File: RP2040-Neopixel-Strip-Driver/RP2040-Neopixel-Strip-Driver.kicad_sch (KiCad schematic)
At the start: 0 parts

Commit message: Added Motor Driver
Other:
- added sheet Motor Driver (DRV8837CDSGR.kicad_sch)
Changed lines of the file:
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@@
+    )
+  )
+  (sheet (at 144.78 130.81) (size 57.15 31.75) (fields_autoplaced)
+    (stroke (width 0.1524) (type solid) (color 0 0 0 0))
+    (fill (color 0 0 0 0.0000))
+    (property "Sheet name" "Motor Driver" (id 0) (at 144.78 130.0984 0)
+      (effects (font (size 1.27 1.27)) (justify left bottom))
+    )
+    (property "Sheet file" "DRV8837CDSGR.kicad_sch" (id 1) (at 144.78 163.1446 0)
+      (effects (font (size 1.27 1.27)) (justify left top))
     )
   )
@@
     (path "/7d3ce60b-0fbc-4d1c-8ad6-57910cd4368e" (page "7"))
     (path "/84db7bec-6432-452c-8477-921546ad9ffb" (page "8"))
+    (path "/855ed567-09e1-4ac3-90b0-f7e25f211a13" (page "9"))
   )
   (symbol_instances
@@
       (reference "U?") (unit 1) (value "S15OT421-005") (footprint "")
     )
+    (path "/855ed567-09e1-4ac3-90b0-f7e25f211a13/a4fd550c-a752-48e0-8fc2-29b1df7424eb"
+      (reference "U?") (unit 1) (value "DRV8837CDSGR") (footprint "SON50P200X200X80-9N")
+    )
     (path "/70fbb85f-3163-4abc-9c0a-a891d94f22b1/cdfffdd0-a453-4bd1-a6a1-94448da82674"

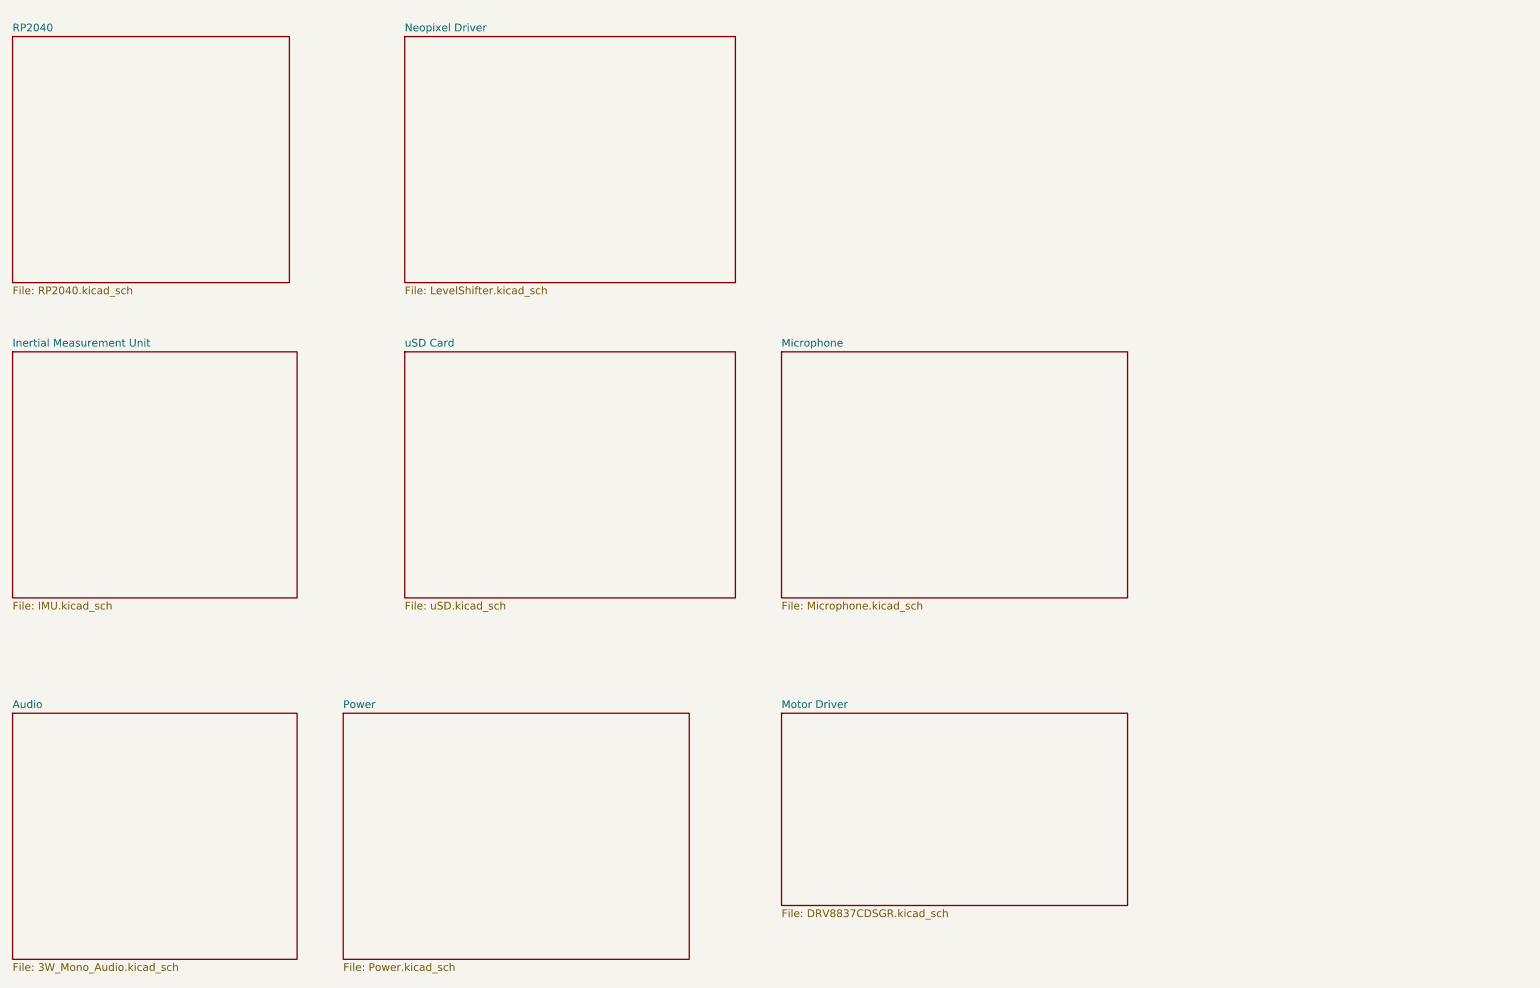
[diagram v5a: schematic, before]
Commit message: Changed name of sheet.
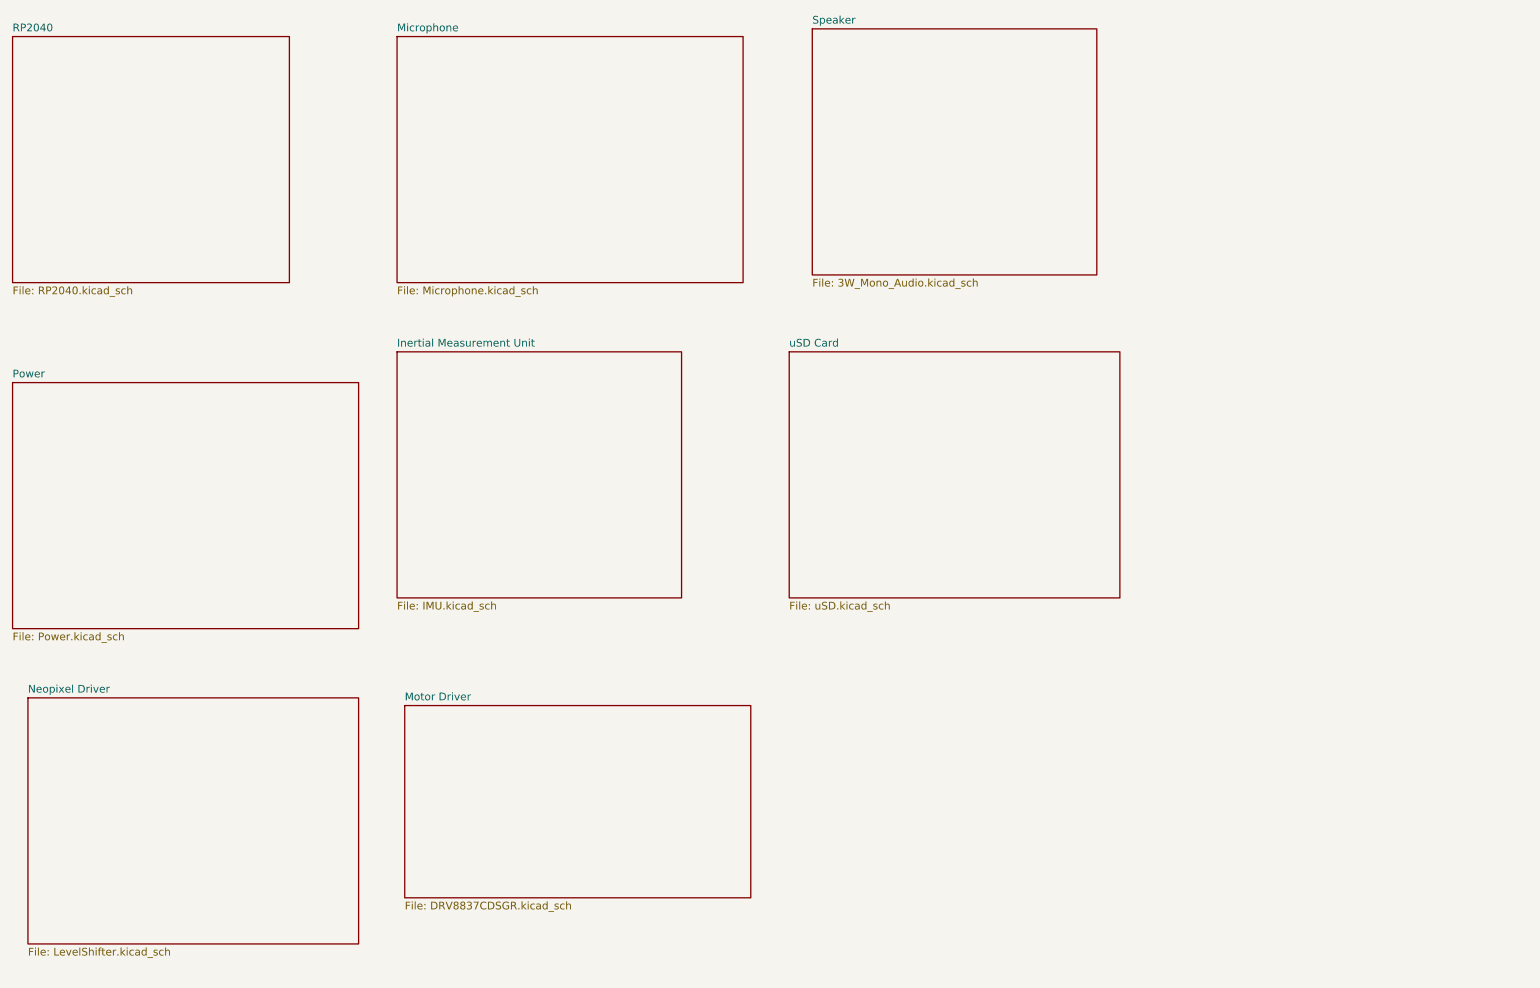
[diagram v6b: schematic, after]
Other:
- sheet Audio renamed Speaker
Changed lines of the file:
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@@
     (comment 4 "https://github.com/mrangen/RP2040-Dev-Board")
   )
-  (sheet (at 17.78 130.81) (size 46.99 40.64) (fields_autoplaced)
+  (sheet (at 149.86 17.78) (size 46.99 40.64) (fields_autoplaced)
     (stroke (width 0.1524) (type solid) (color 0 0 0 0))
     (fill (color 0 0 0 0.0000))
-    (property "Sheet name" "Audio" (id 0) (at 17.78 130.0984 0)
+    (property "Sheet name" "Speaker" (id 0) (at 149.86 17.0684 0)
       (effects (font (size 1.27 1.27)) (justify left bottom))
     )
-    (property "Sheet file" "3W_Mono_Audio.kicad_sch" (id 1) (at 17.78 172.0346 0)
+    (property "Sheet file" "3W_Mono_Audio.kicad_sch" (id 1) (at 149.86 59.0046 0)
       (effects (font (size 1.27 1.27)) (justify left top))
     )
   )
-  (sheet (at 72.39 130.81) (size 57.15 40.64) (fields_autoplaced)
+  (sheet (at 17.78 76.2) (size 57.15 40.64) (fields_autoplaced)
     (stroke (width 0.1524) (type solid) (color 0 0 0 0))
     (fill (color 0 0 0 0.0000))
-    (property "Sheet name" "Power" (id 0) (at 72.39 130.0984 0)
+    (property "Sheet name" "Power" (id 0) (at 17.78 75.4884 0)
       (effects (font (size 1.27 1.27)) (justify left bottom))
     )
-    (property "Sheet file" "Power.kicad_sch" (id 1) (at 72.39 172.0346 0)
+    (property "Sheet file" "Power.kicad_sch" (id 1) (at 17.78 117.4246 0)
       (effects (font (size 1.27 1.27)) (justify left top))
     )
@@
     )
   )
-  (sheet (at 17.78 71.12) (size 46.99 40.64) (fields_autoplaced)
+  (sheet (at 81.28 71.12) (size 46.99 40.64) (fields_autoplaced)
     (stroke (width 0.1524) (type solid) (color 0 0 0 0))
     (fill (color 0 0 0 0.0000))
-    (property "Sheet name" "Inertial Measurement Unit" (id 0) (at 17.78 70.4084 0)
+    (property "Sheet name" "Inertial Measurement Unit" (id 0) (at 81.28 70.4084 0)
       (effects (font (size 1.27 1.27)) (justify left bottom))
     )
-    (property "Sheet file" "IMU.kicad_sch" (id 1) (at 17.78 112.3446 0)
+    (property "Sheet file" "IMU.kicad_sch" (id 1) (at 81.28 112.3446 0)
       (effects (font (size 1.27 1.27)) (justify left top))
     )
   )
-  (sheet (at 82.55 19.05) (size 54.61 40.64) (fields_autoplaced)
+  (sheet (at 20.32 128.27) (size 54.61 40.64) (fields_autoplaced)
     (stroke (width 0.1524) (type solid) (color 0 0 0 0))
     (fill (color 0 0 0 0.0000))
-    (property "Sheet name" "Neopixel Driver" (id 0) (at 82.55 18.3384 0)
+    (property "Sheet name" "Neopixel Driver" (id 0) (at 20.32 127.5584 0)
       (effects (font (size 1.27 1.27)) (justify left bottom))
     )
-    (property "Sheet file" "LevelShifter.kicad_sch" (id 1) (at 82.55 60.2746 0)
+    (property "Sheet file" "LevelShifter.kicad_sch" (id 1) (at 20.32 169.4946 0)
       (effects (font (size 1.27 1.27)) (justify left top))
     )
   )
-  (sheet (at 144.78 71.12) (size 57.15 40.64) (fields_autoplaced)
+  (sheet (at 81.28 19.05) (size 57.15 40.64) (fields_autoplaced)
     (stroke (width 0.1524) (type solid) (color 0 0 0 0))
     (fill (color 0 0 0 0.0000))
-    (property "Sheet name" "Microphone" (id 0) (at 144.78 70.4084 0)
+    (property "Sheet name" "Microphone" (id 0) (at 81.28 18.3384 0)
       (effects (font (size 1.27 1.27)) (justify left bottom))
     )
-    (property "Sheet file" "Microphone.kicad_sch" (id 1) (at 144.78 112.3446 0)
+    (property "Sheet file" "Microphone.kicad_sch" (id 1) (at 81.28 60.2746 0)
       (effects (font (size 1.27 1.27)) (justify left top))
     )
   )
-  (sheet (at 144.78 130.81) (size 57.15 31.75) (fields_autoplaced)
+  (sheet (at 82.55 129.54) (size 57.15 31.75) (fields_autoplaced)
     (stroke (width 0.1524) (type solid) (color 0 0 0 0))
     (fill (color 0 0 0 0.0000))
-    (property "Sheet name" "Motor Driver" (id 0) (at 144.78 130.0984 0)
+    (property "Sheet name" "Motor Driver" (id 0) (at 82.55 128.8284 0)
       (effects (font (size 1.27 1.27)) (justify left bottom))
     )
-    (property "Sheet file" "DRV8837CDSGR.kicad_sch" (id 1) (at 144.78 163.1446 0)
+    (property "Sheet file" "DRV8837CDSGR.kicad_sch" (id 1) (at 82.55 161.8746 0)
       (effects (font (size 1.27 1.27)) (justify left top))
     )
   )
-  (sheet (at 82.55 71.12) (size 54.61 40.64) (fields_autoplaced)
+  (sheet (at 146.05 71.12) (size 54.61 40.64) (fields_autoplaced)
     (stroke (width 0.1524) (type solid) (color 0 0 0 0))
     (fill (color 0 0 0 0.0000))
-    (property "Sheet name" "uSD Card" (id 0) (at 82.55 70.4084 0)
+    (property "Sheet name" "uSD Card" (id 0) (at 146.05 70.4084 0)
       (effects (font (size 1.27 1.27)) (justify left bottom))
     )
-    (property "Sheet file" "uSD.kicad_sch" (id 1) (at 82.55 112.3446 0)
+    (property "Sheet file" "uSD.kicad_sch" (id 1) (at 146.05 112.3446 0)
       (effects (font (size 1.27 1.27)) (justify left top))
     )

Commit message: Added Pico W
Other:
- added sheet Pico W (Pico_W.kicad_sch)
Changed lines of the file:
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@@
+    )
+  )
+  (sheet (at 215.9 17.78) (size 52.07 40.64) (fields_autoplaced)
+    (stroke (width 0.1524) (type solid) (color 0 0 0 0))
+    (fill (color 0 0 0 0.0000))
+    (property "Sheet name" "Pico W" (id 0) (at 215.9 17.0684 0)
+      (effects (font (size 1.27 1.27)) (justify left bottom))
+    )
+    (property "Sheet file" "Pico_W.kicad_sch" (id 1) (at 215.9 59.0046 0)
+      (effects (font (size 1.27 1.27)) (justify left top))
     )
   )
@@
     (path "/84db7bec-6432-452c-8477-921546ad9ffb" (page "8"))
     (path "/855ed567-09e1-4ac3-90b0-f7e25f211a13" (page "9"))
+    (path "/9eb4c32c-a62b-416a-a386-ea1abd0b0a0d" (page "10"))
   )
   (symbol_instances
@@
       (reference "U401") (unit 1) (value "NS4150B") (footprint "Package_SO:MSOP-8-1EP_3x3mm_P0.65mm_EP1.73x1.85mm_ThermalVias")
     )
+    (path "/9eb4c32c-a62b-416a-a386-ea1abd0b0a0d/24ac02ec-8a53-456a-a170-281da5659eb0"
+      (reference "U?") (unit 1) (value "PicoW") (footprint "Pico W:RPi_PicoW_SMD_TH")
+    )
     (path "/84db7bec-6432-452c-8477-921546ad9ffb/3ac9fd70-7920-4300-b1d6-7d56e8e9a95e"
